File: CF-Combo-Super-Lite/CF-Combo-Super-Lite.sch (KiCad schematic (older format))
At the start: 22 parts, among them J1 IDE_CONNECTOR, J2 CF Adapter Power, J3 Bus_ISA_8bit, J4 Addresses, J5 Addresses, U1 BIOS FLASH, U2 74HCT245, U3 GAL22V10, U4 DS1315, U5 AS6C4008-55PCN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

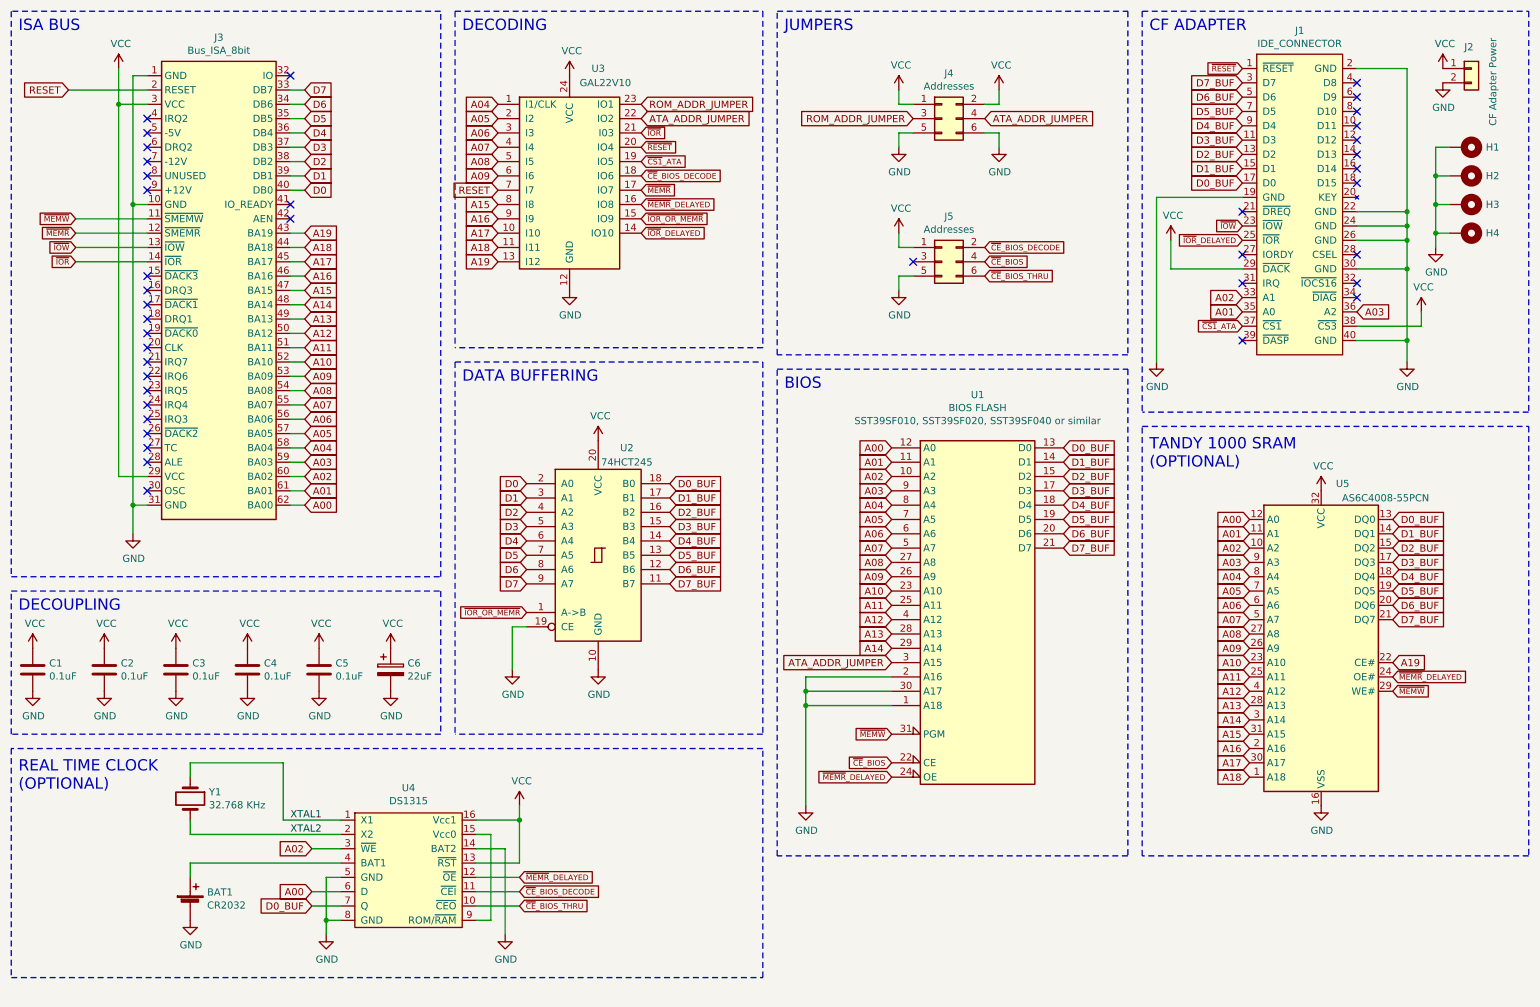
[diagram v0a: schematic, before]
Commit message: CF-Combo-Super-Lite: Add additional bypass cap to CF power. Add back in V20+ jumper (selects different flash ROM range). Add version number. Initial work setting up for JLCPCB production, however they won't assemble boards with edge connectors.
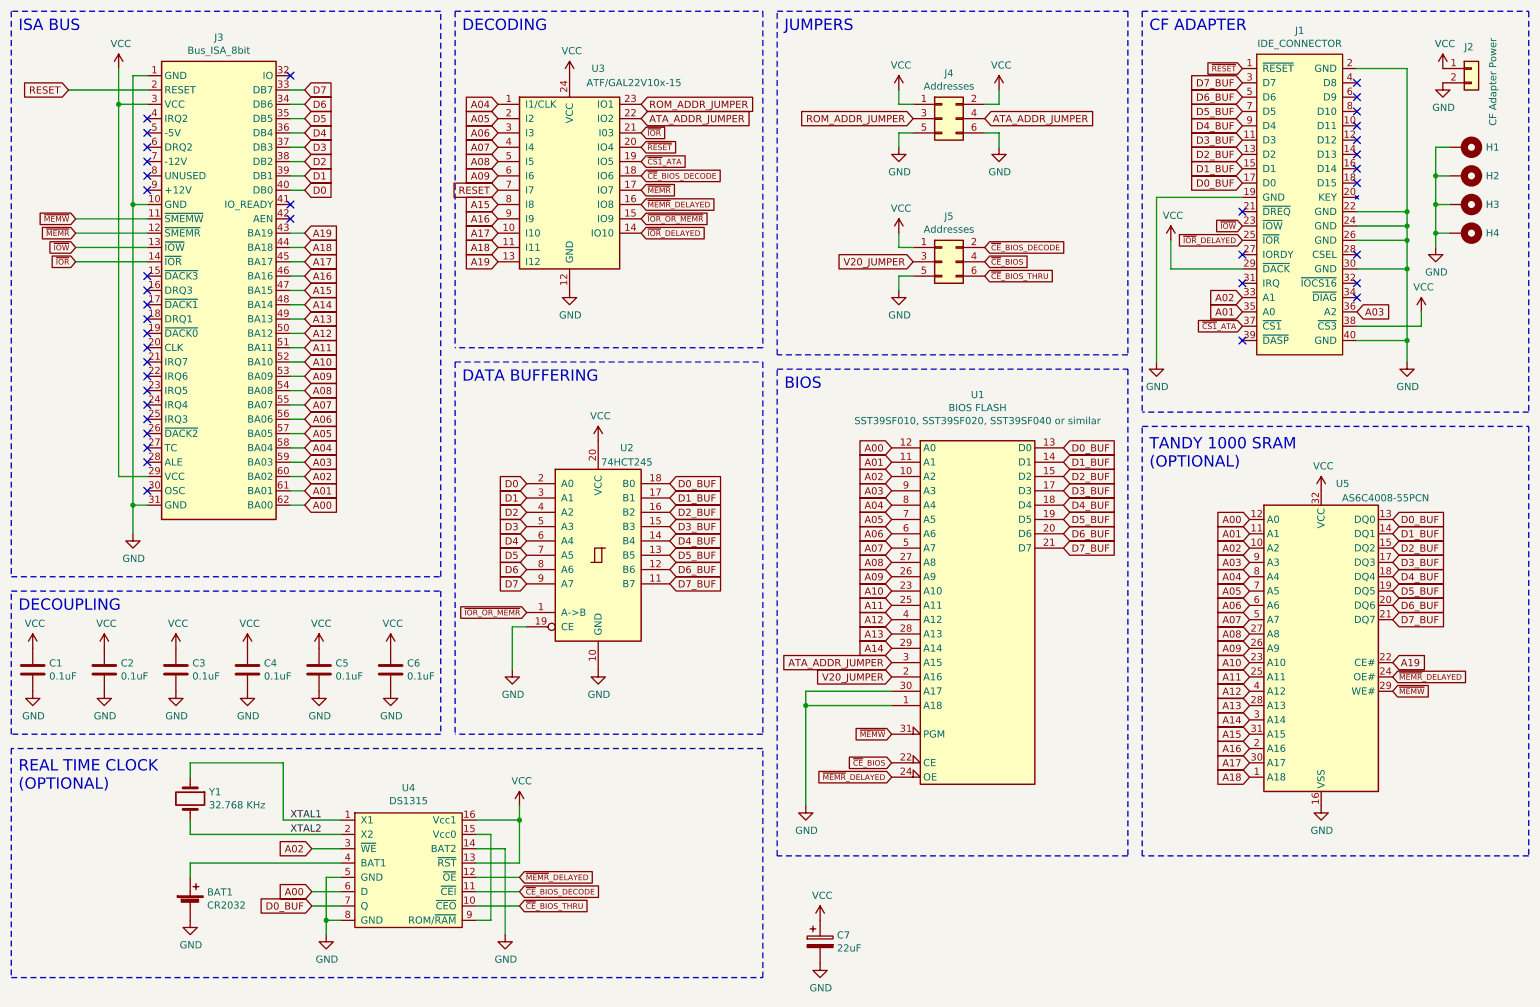
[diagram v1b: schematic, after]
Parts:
- added C6: 0.1uF, Capacitor_THT:C_Disc_D6.0mm_W2.5mm_P5.00mm, symbol Device:C
- C1, C2, C3, C4, C5: LCSC (none) -> C84772; Part options (none) -> C84772,C263183
- U3: value GAL22V10 -> ATF/GAL22V10x-15
- renumbered C6 to C7
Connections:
- net GND: now also C6.2; no longer U1.2 (A16)
- net VCC: now also C6.1
- net V20_JUMPER: now reaches J5.3 (Pin_3)
- net V20_JUMPER: now also U1.2 (A16)
- no-connect marks 40 -> 39
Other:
- moved on the sheet: C7
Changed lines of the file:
@@
 Text GLabel 3950 1900 0    50   Input ~ 0
 A15
-Wire Wire Line
-	6700 5200 6100 5200
-Wire Wire Line
-	6100 5200 6100 5300
 Connection ~ 6100 5400
 Wire Wire Line
 	6700 5300 6100 5300
-Connection ~ 6100 5300
 Wire Wire Line
 	6100 5300 6100 5400
@@
 F 2 "Capacitor_THT:C_Disc_D6.0mm_W2.5mm_P5.00mm" H 738 5000 50  0001 C CNN
 F 3 "~" H 700 5150 50  0001 C CNN
+F 4 "C84772" H 700 5150 50  0001 C CNN "LCSC"
+F 5 "C84772,C263183" H 700 5150 50  0001 C CNN "Part options"
 	1    700  5150
 	1    0    0    -1
@@
 F 2 "Capacitor_THT:C_Disc_D6.0mm_W2.5mm_P5.00mm" H 1238 5000 50  0001 C CNN
 F 3 "~" H 1200 5150 50  0001 C CNN
+F 4 "C84772" H 1200 5150 50  0001 C CNN "LCSC"
+F 5 "C84772,C263183" H 1200 5150 50  0001 C CNN "Part options"
 	1    1200 5150
 	1    0    0    -1
@@
 P 4450 1700
 F 0 "U3" H 4650 2450 50  0000 C CNN
-F 1 "GAL22V10" H 4700 2350 50  0000 C CNN
+F 1 "ATF/GAL22V10x-15" H 4900 2350 50  0000 C CNN
 F 2 "Package_DIP:DIP-24_W7.62mm_Socket" H 4450 1700 50  0001 C CNN
 F 3 "" H 4450 1700 50  0001 C CNN
@@
 F 2 "Capacitor_THT:C_Disc_D6.0mm_W2.5mm_P5.00mm" H 2738 5000 50  0001 C CNN
 F 3 "~" H 2700 5150 50  0001 C CNN
+F 4 "C84772" H 2700 5150 50  0001 C CNN "LCSC"
+F 5 "C84772,C263183" H 2700 5150 50  0001 C CNN "Part options"
 	1    2700 5150
 	1    0    0    -1
@@
 F 2 "Capacitor_THT:C_Disc_D6.0mm_W2.5mm_P5.00mm" H 2238 5000 50  0001 C CNN
 F 3 "~" H 2200 5150 50  0001 C CNN
+F 4 "C84772" H 2200 5150 50  0001 C CNN "LCSC"
+F 5 "C84772,C263183" H 2200 5150 50  0001 C CNN "Part options"
 	1    2200 5150
 	1    0    0    -1
 $EndComp
 $Comp
-L Device:CP C6
+L Device:CP C7
 U 1 1 60440B68
-P 3200 5150
-F 0 "C6" H 3318 5196 50  0000 L CNN
-F 1 "22uF" H 3318 5105 50  0000 L CNN
-F 2 "Capacitor_THT:CP_Radial_D5.0mm_P2.50mm" H 3238 5000 50  0001 C CNN
-F 3 "~" H 3200 5150 50  0001 C CNN
-	1    3200 5150
+P 6200 7050
+F 0 "C7" H 6318 7096 50  0000 L CNN
+F 1 "22uF" H 6318 7005 50  0000 L CNN
+F 2 "Capacitor_THT:CP_Radial_D5.0mm_P2.50mm" H 6238 6900 50  0001 C CNN
+F 3 "~" H 6200 7050 50  0001 C CNN
+	1    6200 7050
 	1    0    0    -1
 $EndComp
@@
 L power:VCC #PWR0122
 U 1 1 6043C274
-P 3200 5000
-F 0 "#PWR0122" H 3200 4850 50  0001 C CNN
-F 1 "VCC" H 3215 5173 50  0000 C CNN
-F 2 "" H 3200 5000 50  0001 C CNN
-F 3 "" H 3200 5000 50  0001 C CNN
-	1    3200 5000
+P 6200 6900
+F 0 "#PWR0122" H 6200 6750 50  0001 C CNN
+F 1 "VCC" H 6215 7073 50  0000 C CNN
+F 2 "" H 6200 6900 50  0001 C CNN
+F 3 "" H 6200 6900 50  0001 C CNN
+	1    6200 6900
 	1    0    0    -1
 $EndComp
@@
 L power:GND #PWR0121
 U 1 1 6043C26A
-P 3200 5300
-F 0 "#PWR0121" H 3200 5050 50  0001 C CNN
-F 1 "GND" H 3205 5127 50  0000 C CNN
-F 2 "" H 3200 5300 50  0001 C CNN
-F 3 "" H 3200 5300 50  0001 C CNN
-	1    3200 5300
+P 6200 7200
+F 0 "#PWR0121" H 6200 6950 50  0001 C CNN
+F 1 "GND" H 6205 7027 50  0000 C CNN
+F 2 "" H 6200 7200 50  0001 C CNN
+F 3 "" H 6200 7200 50  0001 C CNN
+	1    6200 7200
 	1    0    0    -1
 $EndComp
@@
 F 2 "Capacitor_THT:C_Disc_D6.0mm_W2.5mm_P5.00mm" H 1738 5000 50  0001 C CNN
 F 3 "~" H 1700 5150 50  0001 C CNN
+F 4 "C84772" H 1700 5150 50  0001 C CNN "LCSC"
+F 5 "C84772,C263183" H 1700 5150 50  0001 C CNN "Part options"
 	1    1700 5150
 	1    0    0    -1
@@
 Text GLabel 7350 2400 2    39   Input ~ 0
 ~CE~_BIOS_THRU
-NoConn ~ 6850 2300
-$Comp
-L power:GND #PWR?
+$Comp
+L power:GND #PWR0139
 U 1 1 60ED8F42
 P 10550 1050
-F 0 "#PWR?" H 10550 800 50  0001 C CNN
+F 0 "#PWR0139" H 10550 800 50  0001 C CNN
 F 1 "GND" H 10555 877 50  0000 C CNN
 F 2 "" H 10550 1050 50  0001 C CNN
@@
 	1    0    0    -1
 $EndComp
+$Comp
+L power:VCC #PWR0140
+U 1 1 6127AA7C
+P 3200 5000
+F 0 "#PWR0140" H 3200 4850 50  0001 C CNN
+F 1 "VCC" H 3215 5173 50  0000 C CNN
+F 2 "" H 3200 5000 50  0001 C CNN
+F 3 "" H 3200 5000 50  0001 C CNN
+	1    3200 5000
+	1    0    0    -1
+$EndComp
+$Comp
+L power:GND #PWR0141
+U 1 1 6127AFFE
+P 3200 5300
+F 0 "#PWR0141" H 3200 5050 50  0001 C CNN
+F 1 "GND" H 3205 5127 50  0000 C CNN
+F 2 "" H 3200 5300 50  0001 C CNN
+F 3 "" H 3200 5300 50  0001 C CNN
+	1    3200 5300
+	1    0    0    -1
+$EndComp
+$Comp
+L Device:C C6
+U 1 1 6127B008
+P 3200 5150
+F 0 "C6" H 3315 5196 50  0000 L CNN
+F 1 "0.1uF" H 3315 5105 50  0000 L CNN
+F 2 "Capacitor_THT:C_Disc_D6.0mm_W2.5mm_P5.00mm" H 3238 5000 50  0001 C CNN
+F 3 "~" H 3200 5150 50  0001 C CNN
+F 4 "C84772" H 3200 5150 50  0001 C CNN "LCSC"
+F 5 "C84772,C263183" H 3200 5150 50  0001 C CNN "Part options"
+	1    3200 5150
+	1    0    0    -1
+$EndComp
+Text GLabel 6850 2300 0    50   Input ~ 0
+V20_JUMPER
+Text GLabel 6700 5200 0    50   Input ~ 0
+V20_JUMPER
 $EndSCHEMATC
